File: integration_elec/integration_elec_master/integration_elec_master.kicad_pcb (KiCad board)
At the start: 4 copper layers, 135.5 x 140 mm, 62 parts, among them J2 USB_C_Receptacle_USB2.0_16P, Q1 Q_NMOS_GSD, SW1 SW_Push, U2 STM32F446RETx, U3 USBLC6-2SC6, U4 TPS54335ADDAR, U5 COM-28379, U6 COM-09032

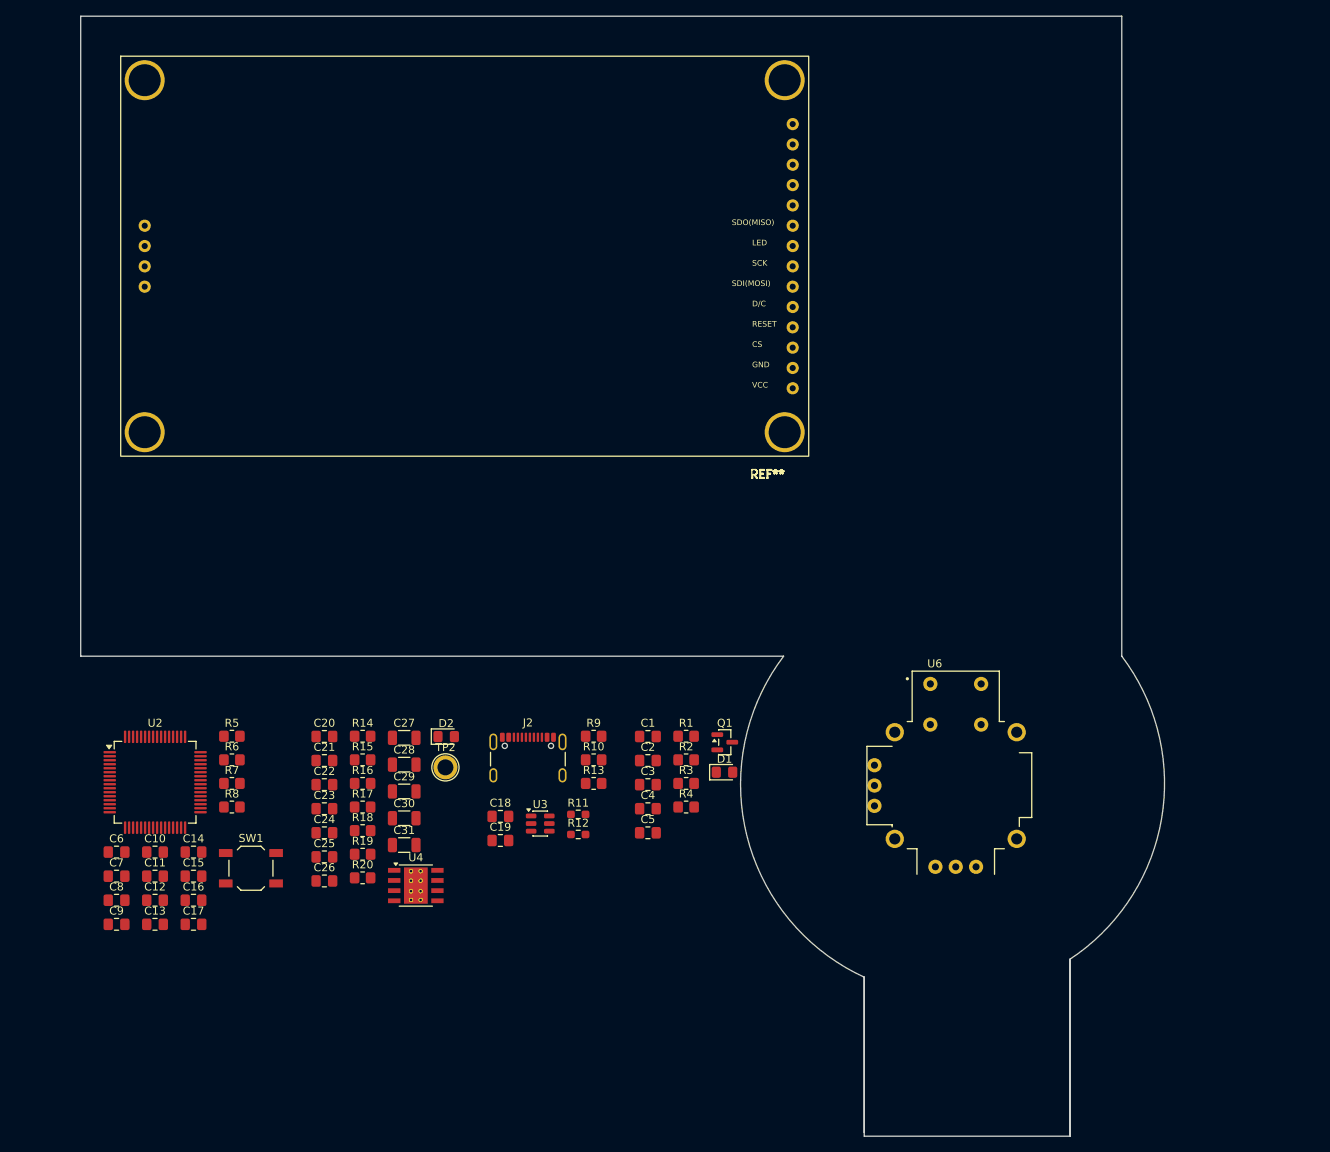
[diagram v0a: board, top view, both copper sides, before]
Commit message: Added switch in design + Footprint + symbol
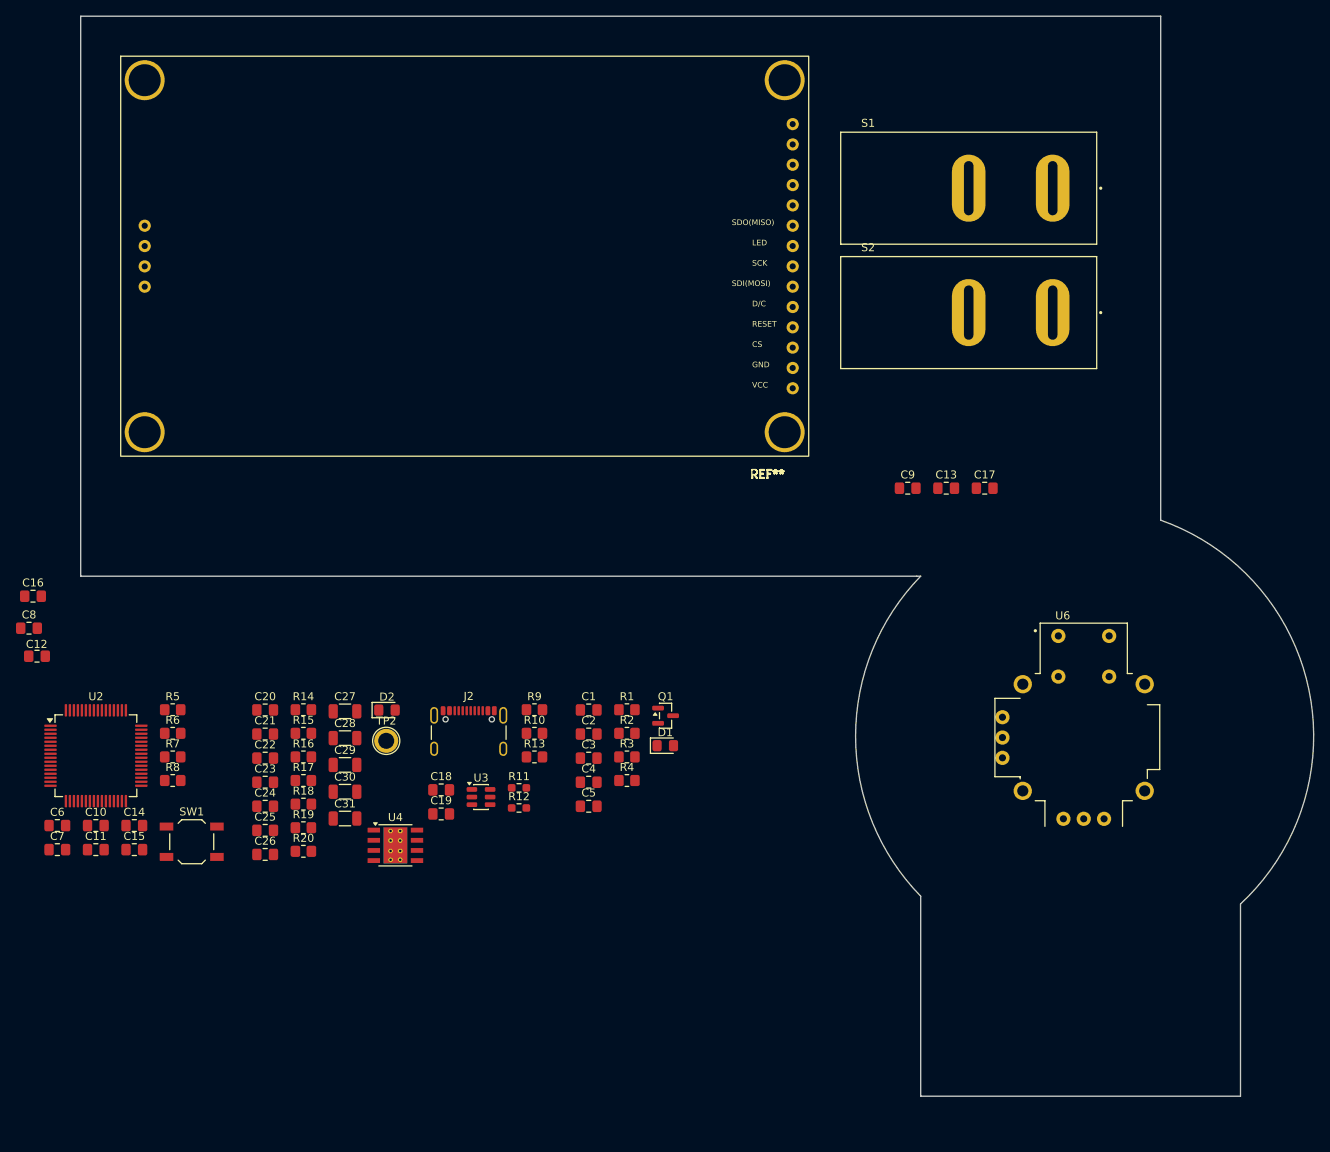
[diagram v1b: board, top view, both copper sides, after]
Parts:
- added S1: RB141C1100, SWITCH:SW_RB141C1100, F.Cu at (181.0, 46.5)
- added S2: RB141C1100, SWITCH:SW_RB141C1100, F.Cu at (181.0, 62.0)
- moved C17 112.9 mm to (183.0, 84.0)
- moved C13 112.9 mm to (178.2, 84.0)
- moved C9 112.9 mm to (173.4, 84.0)
- moved C16 43.0 mm to (64.0, 97.5)
- moved C8 35.7 mm to (63.5, 101.5)
- moved C12 33.9 mm to (64.5, 105.0)
- moved U6 17.1 mm to (195.4, 115.2)
- moved C10 8.11 mm to (71.9, 126.2)
- moved C3 8.11 mm to (133.5, 117.7)
- moved C6 8.11 mm to (67.1, 126.2)
- moved C1 8.11 mm to (133.5, 111.7)
- moved C11 8.11 mm to (71.9, 129.2)
- moved C2 8.11 mm to (133.5, 114.7)
- moved C4 8.11 mm to (133.5, 120.8)
- moved C5 8.11 mm to (133.5, 123.8)
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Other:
- board size 135.5 x 140 mm -> 154.1 x 135 mm
